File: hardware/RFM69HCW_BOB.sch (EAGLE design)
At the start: 13 parts, among them U1 RFM69HCW

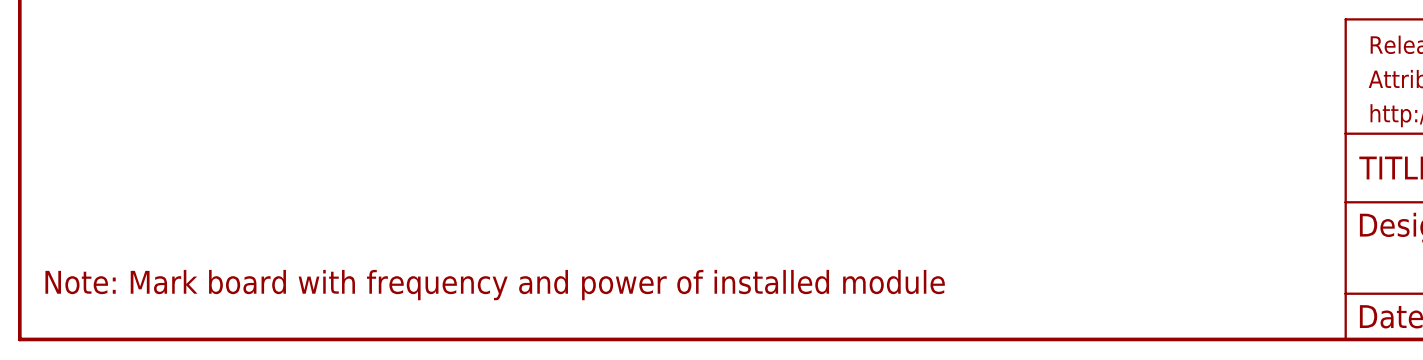
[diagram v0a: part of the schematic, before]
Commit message: Minor silk updates
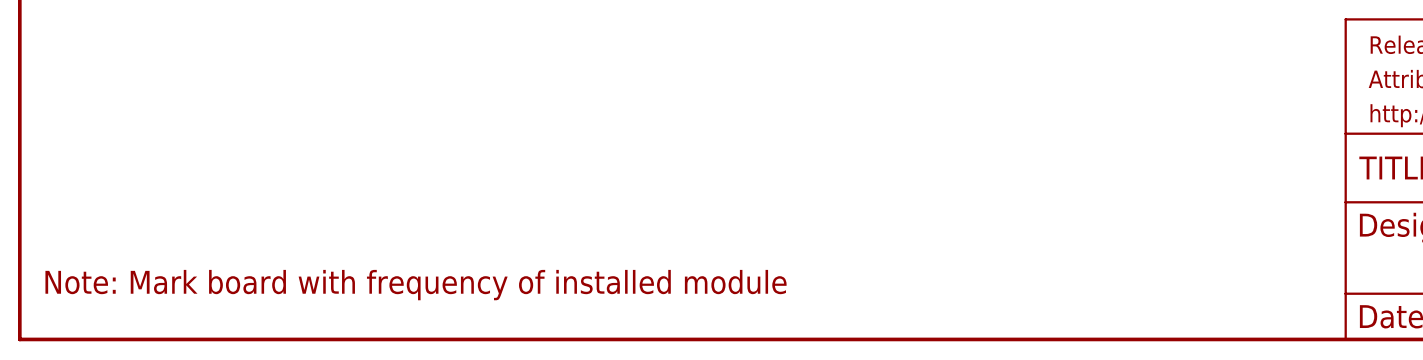
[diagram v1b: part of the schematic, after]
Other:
- note added: "Note: Mark board with frequency of installed module"
- note removed: "Note: Mark board with frequency and power of installed module"
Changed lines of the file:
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@@
 <text x="172.72" y="7.62" size="2.54" layer="94">M Grusin</text>
 <text x="241.3" y="7.62" size="2.54" layer="94">01</text>
-<text x="2.54" y="5.08" size="2.54" layer="94">Note: Mark board with frequency and power of installed module</text>
+<text x="2.54" y="5.08" size="2.54" layer="94">Note: Mark board with frequency of installed module</text>
 <text x="175.26" y="91.44" size="2.54" layer="94">Antenna length (1/4 wave)
 915MHz: 3.07" = 78mm
